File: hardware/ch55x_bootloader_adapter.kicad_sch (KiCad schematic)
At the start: 7 parts

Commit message: more hardware progress
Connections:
- net SBU1: no longer names the net of USB_C_PLUG1.A8 (SBU1)
- net SBU1: no longer USB_C_RECEPTABLE1.A8 (SBU1)
- net SBU2: no longer names the net of USB_C_PLUG1.B8 (SBU2)
- net SBU2: no longer USB_C_RECEPTABLE1.B8 (SBU2)
- no-connect marks 8 -> 12
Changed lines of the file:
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@@
-	)
-	(junction
-		(at 173.99 27.94)
-		(diameter 0)
-		(color 0 0 0 0)
 	)
 	(junction
@@
 	)
 	(no_connect
+		(at 49.53 78.74)
+	)
+	(no_connect
+		(at 173.99 83.82)
+	)
+	(no_connect
 		(at 173.99 55.88)
 	)
 	(no_connect
+		(at 49.53 76.2)
+	)
+	(no_connect
 		(at 173.99 60.96)
 	)
+	(no_connect
+		(at 173.99 86.36)
+	)
 	(wire
 		(pts
@@
 			(width 0)
 			(type default)
-		)
-	)
-	(label "SBU1"
-		(at 49.53 76.2 0)
-		(effects
-			(font
-				(size 1.27 1.27)
-			)
-			(justify left bottom)
 		)
 	)
@@
 		)
 	)
-	(label "GND"
-		(at 152.4 86.36 0)
-		(effects
-			(font
-				(size 1.27 1.27)
-			)
-			(justify left bottom)
-		)
-	)
 	(label "CC1"
 		(at 173.99 33.02 0)
@@
 		)
 	)
-	(label "SBU2"
-		(at 49.53 78.74 0)
-		(effects
-			(font
-				(size 1.27 1.27)
-			)
-			(justify left bottom)
-		)
-	)
 	(label "GND"
 		(at 26.67 86.36 0)
@@
 		)
 	)
-	(label "SBU2"
-		(at 173.99 86.36 0)
-		(effects
-			(font
-				(size 1.27 1.27)
-			)
-			(justify left bottom)
-		)
-	)
 	(label "GND"
 		(at 158.75 93.98 0)
@@
 		(effects
 			(font
-				(size 1.27 1.27)
-			)
-			(justify left bottom)
-		)
-	)
-	(label "SBU1"
-		(at 173.99 83.82 0)
-		(effects
-			(font

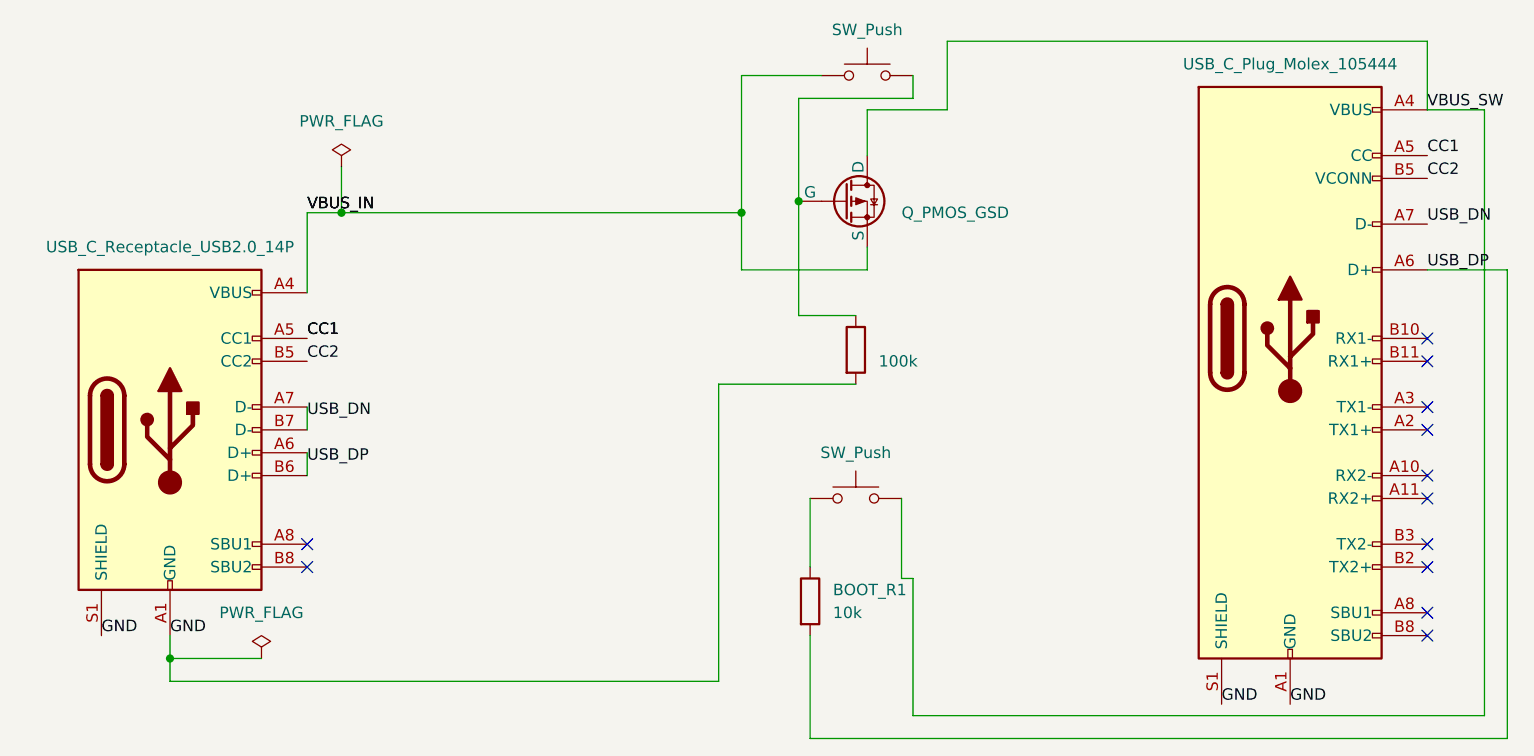
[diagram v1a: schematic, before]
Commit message: change adapter to be USB-A instead for simplicity and cost
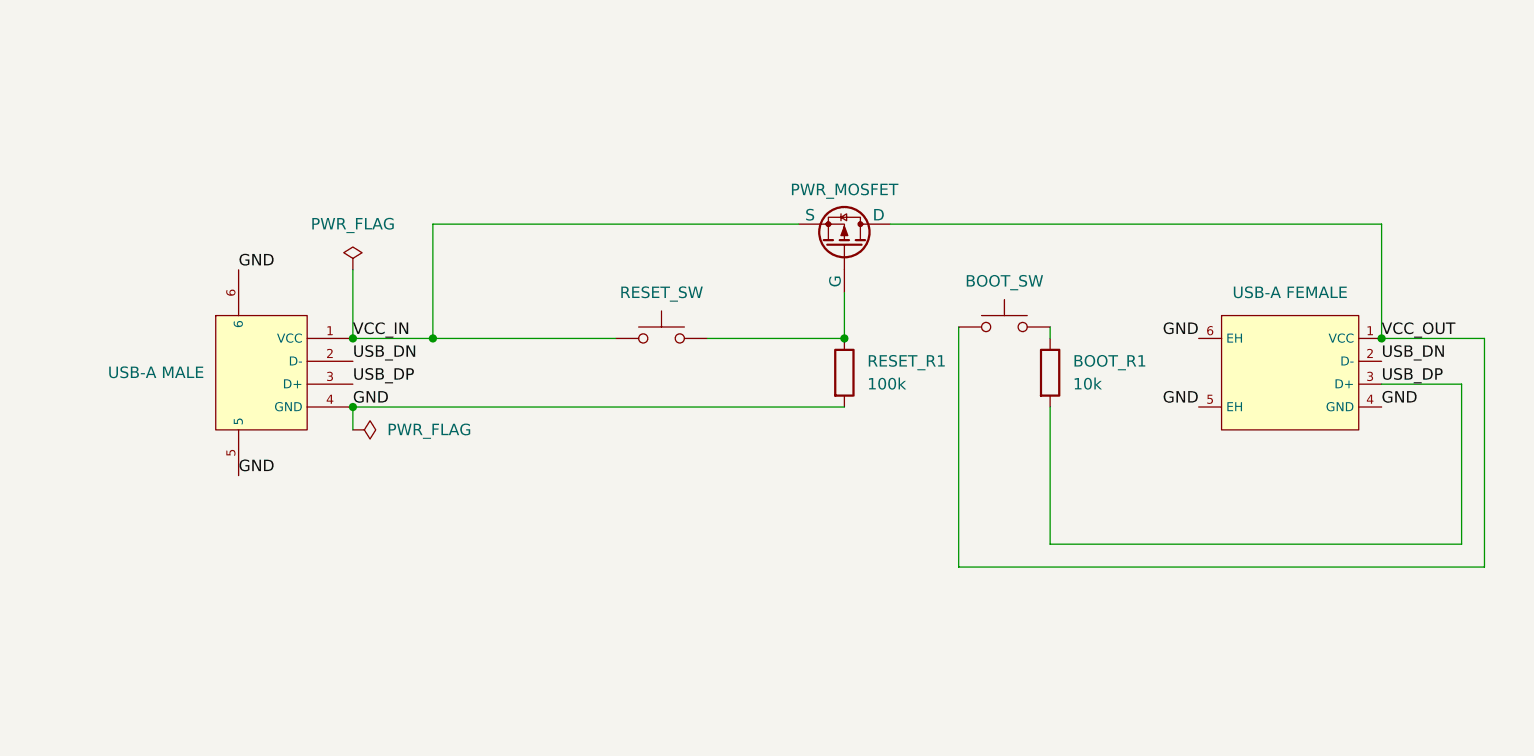
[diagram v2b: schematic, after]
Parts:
- removed USB_C_PLUG1: USB_C_Plug_Molex_105444, Connector_USB:USB_C_Plug_Molex_105444, symbol Connector:USB_C_Plug
- removed USB_C_RECEPTABLE1: USB_C_Receptacle_USB2.0_14P, Connector_USB:USB_C_Receptacle_GCT_USB4105-xx-A_16P_TopMnt_Horizontal, symbol Connector:USB_C_Receptacle_USB2.0_16P
- added U1: USB-A MALE, jlc:USB-A-TH_U-G-04WD-W-01, symbol JLC2KiCad:U-G-04DD-W-01
- added USB1: USB-A FEMALE, jlc:USB-A-SMD_U-A-24SS-W-2, symbol JLC2KiCad:U-A-24SS-W-2
- BOOT1: value SW_Push -> BOOT_SW
- RESET1: value SW_Push -> RESET_SW
- RESET_MOSFET1: value Q_PMOS_GSD -> PWR_MOSFET
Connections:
- net GND: now also U1.4 (GND), U1.5, U1.6, USB1.4 (GND), USB1.5 (EH), USB1.6 (EH)
- net USB_DN: now also U1.2 (D-), USB1.2 (D-)
- net USB_DP: now also U1.3 (D+), USB1.3 (D+)
- net at BOOT_R1.1: now also BOOT1.2; no longer BOOT1.1
- net VBUS_IN renamed VCC_IN
- net VCC_IN: now also U1.1 (VCC)
- net VBUS_SW renamed VCC_OUT
- net VCC_OUT: now also BOOT1.1, USB1.1 (VCC); no longer BOOT1.2
- no-connect marks 12 -> 0
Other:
- moved on the sheet: BOOT_R1

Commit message: swap to new buttons and improve layout further
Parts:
- BOOT1, RESET1: footprint Button_Switch_SMD:SW_Push_1P1T_NO_CK_KSC7xxJ -> jlc:SW-SMD_4P-L6.2-W6.2-P4.00-LS9.5-TL
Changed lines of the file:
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@@
 			)
 		)
-		(property "Footprint" "Button_Switch_SMD:SW_Push_1P1T_NO_CK_KSC7xxJ"
+		(property "Footprint" "jlc:SW-SMD_4P-L6.2-W6.2-P4.00-LS9.5-TL"
 			(at 127 46.99 0)
 			(effects
@@
 			)
 		)
-		(property "Footprint" "Button_Switch_SMD:SW_Push_1P1T_NO_CK_KSC7xxJ"
+		(property "Footprint" "jlc:SW-SMD_4P-L6.2-W6.2-P4.00-LS9.5-TL"
 			(at 88.9 48.26 0)
 			(effects

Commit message: minor tweaks to adapter, added instructions on back of it
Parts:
- renumbered USB1 to USB-A-F1, U1 to USB-A-M1
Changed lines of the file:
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@@
 		(dnp no)
 		(fields_autoplaced yes)
-		(property "Reference" "USB1"
+		(property "Reference" "USB-A-F1"
 			(at 158.75 45.72 0)
 			(effects
@@
 			(project ""
 				(path "/16bf942e-60cf-44bb-b9e1-b94d352868d6"
-					(reference "USB1")
+					(reference "USB-A-F1")
 					(unit 1)
 				)
@@
 		(dnp no)
 		(fields_autoplaced yes)
-		(property "Reference" "U1"
+		(property "Reference" "USB-A-M1"
 			(at 38.1 55.8799 0)
 			(effects
@@
 			(project ""
 				(path "/16bf942e-60cf-44bb-b9e1-b94d352868d6"
-					(reference "U1")
-					(unit 1)
-				)
+					(reference "USB-A-M1")
+					(unit 1)
+				)
